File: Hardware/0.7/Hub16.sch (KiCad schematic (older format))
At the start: 97 parts, among them J1 USB_C_Receptacle_USB2.0, J2 AVR-ISP-6, K1 KEYSW, K11 KEYSW, K12 KEYSW, K13 KEYSW, K14 KEYSW, K16 KEYSW, K17 KEYSW, K18 KEYSW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

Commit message: update footprints + bom
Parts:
- C1: DigiKey 1276-1871-1-ND -> 1276-1871-1-ND; LCSC C85713 -> C85713; MPN CL10A106MP8NNNC -> CL10A106MP8NNNC; Substitue Allowed? Y -> Y - X5R or better
- C10, C11, C38, C4, C5, C6, C7, C8, C9: Substitue Allowed? Y -> Y - X5R or better
- C2, C3: value 22p -> 15p; DigiKey 1276-2228-1-ND -> 1276-1296-2-ND; LCSC C1653 -> C1644; MPN CL10C220JB8NFNC -> CL10C150JB8NNNC; Substitue Allowed? Y -> Y - NP0 / C0G or better
- C23, C27, C28, C29, C30, C31, C32, C33, C34, C35, C36, C37: DigiKey (none) -> 1276-1000-1-ND; LCSC (none) -> C1591; MPN (none) -> CL10B104KB8NNNC; Manufacturer (none) -> Samsung Electro-Mechanics; Substitue Allowed? (none) -> Y - X5R or better
- D1: DigiKey 732-4980-1-ND -> (none); MPN 150060VS75000 -> OSK40603C1E; Manufacturer Wurth Electronik -> OptoSupply; Notes LCSC: Substutite PN -> (none); Substitue Allowed? Y -> Y - Any Pink / Purple
- D10, D16, D2, D22, D23, D29, D3, D30, D31, D32, D4: LCSC C114586 -> C268294; Notes (none) -> Black prefered, but white also suitable
- D11, D12, D13, D14, D17, D18, D19, D20, D24, D25, D26, D27, D5, D6, D7, D8: Substitue Allowed? Y -> Y - Any 1N4148
- F1: LCSC C181350 -> C66452; Substitue Allowed? Y -> Y - 500mA hold / 1A trip
- FB5: DigiKey 490-1014-1-ND -> 490-5258-1-ND; LCSC C19330 -> C85833; MPN BLM18AG601SN1D -> BLM18KG601SN1D; Substitue Allowed? Y -> Y - 600R, > 1A current
- J1: Substitue Allowed? Y -> Y - Footprint / pinout compatiable
- R1: DigiKey CR0603-JW-222ELFCT-ND -> 118-CR0603-JW-512ELFCT-ND; LCSC C113303 -> C14677; MPN CR0603-JW-222ELF -> CR0603-JW-512ELF; Substitue Allowed? Y -> Y - Same spec
- R11, R2, R3, R4, R5, R6, R7, R8, RN1, RN3: Substitue Allowed? Y -> Y - Same spec
- SW1: value KMR2 -> EVQPUL; DigiKey 401-1704-1-ND -> P10853SCT-ND; LCSC C354946 -> C397351; MPN KSR223GLFG -> EVQ-PUL02K; Manufacturer C&K -> Panasonic; Substitue Allowed? Y -> Y - Same footprint
- SW2, SW3: DigiKey 987-1398-ND -> PEC11L-4120F-S0020-ND; LCSC C361165 -> (none); MPN EC11E1834403 -> PEC11L-4120F-S0020; Manufacturer (none) -> Bourns; Substitue Allowed? Y -> Y - 20 PPR
- U2: DigiKey ATMEGA32U4-AURCT-ND -> ATMEGA32U4-MU-ND; LCSC C44854 -> C45874; MPN ATMEGA32U4-AU -> ATMEGA32U4-MU
- Y1: DigiKey 535-9134-1-ND -> 535-9675-6-ND; LCSC C179641 -> C164044; MPN ABM8-16.000MHZ-B2-T -> ABM8-16.000MHZ-10-1-U-T; Notes (none) -> LCSC: Substitute PN; Substitue Allowed? Y -> Y - 16 MHz, 10/12pF

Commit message: add note on uncommenting out code
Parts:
- C2, C3: Substitue Allowed? Y - NP0 / C0G or better -> Y - NP0 / C0G
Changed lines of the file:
@@
 F 4 "1276-1296-2-ND" H 2875 3325 50  0001 C CNN "DigiKey"
 F 5 "CL10C150JB8NNNC" H 2875 3325 50  0001 C CNN "MPN"
-F 6 "Y - NP0 / C0G or better" H 2875 3325 50  0001 C CNN "Substitue Allowed?"
+F 6 "Y - NP0 / C0G" H 2875 3325 50  0001 C CNN "Substitue Allowed?"
 F 7 "C1644" H 2875 3325 50  0001 C CNN "LCSC"
 F 8 "Samsung Electro-Mechanics" H 2875 3325 50  0001 C CNN "Manufacturer"
@@
 F 4 "1276-1296-2-ND" H 2875 2925 50  0001 C CNN "DigiKey"
 F 5 "CL10C150JB8NNNC" H 2875 2925 50  0001 C CNN "MPN"
-F 6 "Y - NP0 / C0G or better" H 2875 2925 50  0001 C CNN "Substitue Allowed?"
+F 6 "Y - NP0 / C0G" H 2875 2925 50  0001 C CNN "Substitue Allowed?"
 F 7 "C1644" H 2875 2925 50  0001 C CNN "LCSC"
 F 8 "Samsung Electro-Mechanics" H 2875 2925 50  0001 C CNN "Manufacturer"

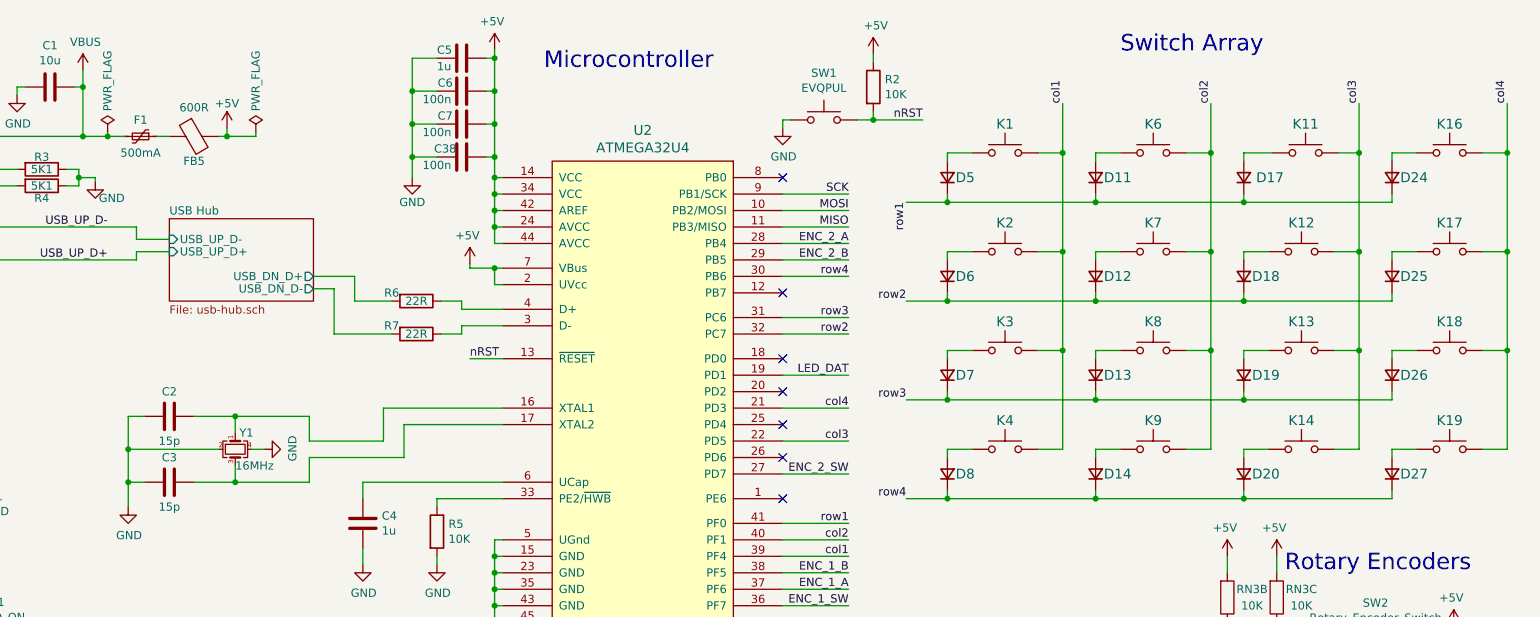
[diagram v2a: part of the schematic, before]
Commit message: update fuse values
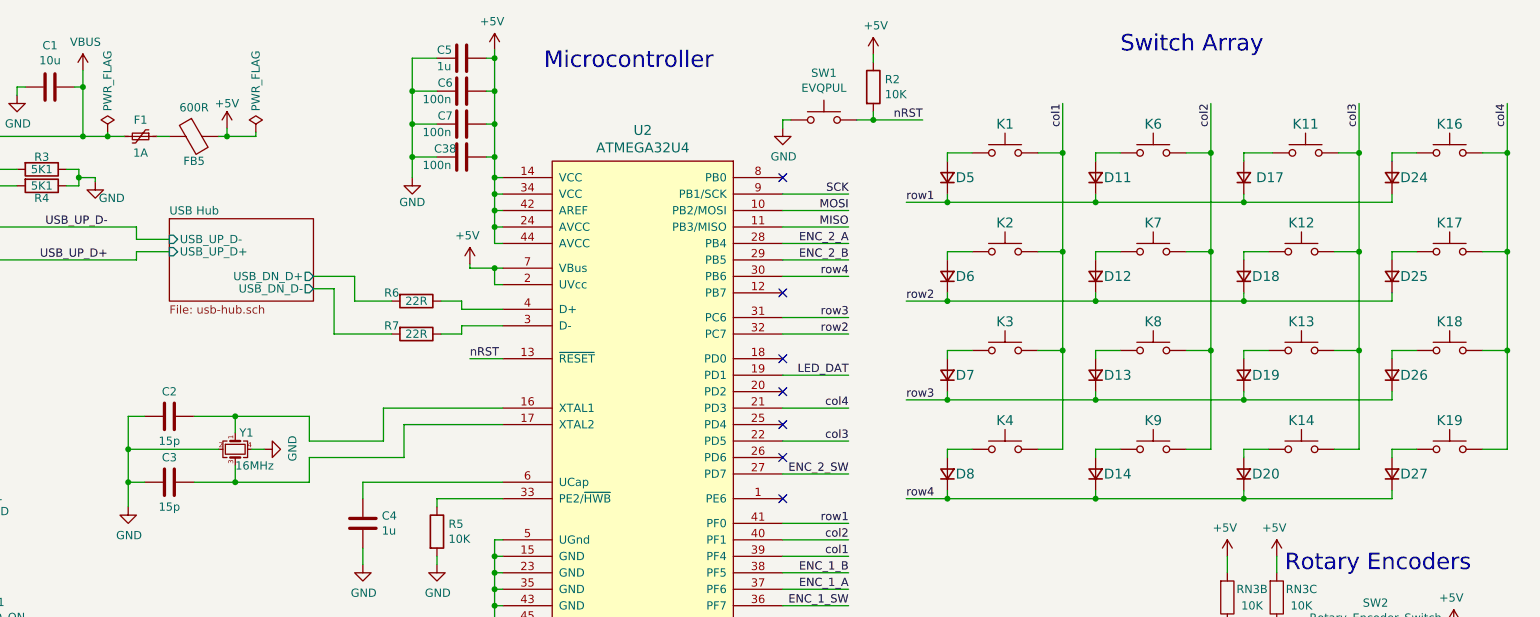
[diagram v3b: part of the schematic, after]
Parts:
- D1: Notes (none) -> Cannot source from DigiKey
- F1: value 500mA -> 1A; DigiKey 507-1813-1-ND -> F2774CT-ND; LCSC C66452 -> C80270; MPN 0ZCK0050FF2E -> 0805L100WR; Manufacturer Bel Fuse -> Littelfuse; Notes LCSC: Substitute PN -> (none); Substitue Allowed? Y - 500mA hold / 1A trip -> Y - 1A hold / >1.5A trip
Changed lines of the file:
@@
 	8500 2825 9400 2825
 Connection ~ 9400 2825
-Text Label 7350 2825 2    50   ~ 0
+Text Label 7350 2825 0    50   ~ 0
 row3
 Text Notes 8650 725  0    100  ~ 0
@@
 row4
 Connection ~ 2625 3325
-Text Label 11000 1025 1    50   ~ 0
+Text Label 11000 1025 3    50   ~ 0
 col4
-Text Label 10100 1025 1    50   ~ 0
+Text Label 10100 1025 3    50   ~ 0
 col3
-Text Label 9200 1025 1    50   ~ 0
+Text Label 9200 1025 3    50   ~ 0
 col2
-Text Label 8300 1025 1    50   ~ 0
+Text Label 8300 1025 3    50   ~ 0
 col1
 $Comp
@@
 Wire Wire Line
 	7600 1925 7600 1975
-Text Label 7350 2225 2    50   ~ 0
+Text Label 7350 2225 0    50   ~ 0
 row2
 Connection ~ 9400 2225
@@
 Wire Wire Line
 	7600 1325 7600 1375
-Text Label 7350 1625 3    50   ~ 0
+Text Label 7350 1625 0    50   ~ 0
 row1
 Connection ~ 9400 1625
@@
 Wire Wire Line
 	7600 3125 7600 3175
-Text Label 7350 3425 2    50   ~ 0
+Text Label 7350 3425 0    50   ~ 0
 row4
 Wire Wire Line
@@
 F 8 "C364559" H 1650 3450 50  0001 C CNN "LCSC"
 F 9 "OptoSupply" H 1650 3450 50  0001 C CNN "Manufacturer"
-F 10 "" H 1650 3450 50  0001 C CNN "Notes"
+F 10 "Cannot source from DigiKey" H 1650 3450 50  0001 C CNN "Notes"
 	1    1650 3450
 	0    -1   -1   0
@@
 AR Path="/5E5406D9/5EB49DDF" Ref="F?"  Part="1"
 F 0 "F1" V 2600 1225 50  0000 C CNN
-F 1 "500mA" V 2800 1225 50  0000 C CNN
+F 1 "1A" V 2800 1225 50  0000 C CNN
 F 2 "josh-passives-smt:Fuse_0805_2012Metric" H 2750 1025 50  0001 L CNN
 F 3 "~" H 2700 1225 50  0001 C CNN
-F 4 "C66452" H 2700 1225 50  0001 C CNN "LCSC"
-F 5 "0ZCK0050FF2E" H 2700 1225 50  0001 C CNN "MPN"
-F 6 "507-1813-1-ND" H 2700 1225 50  0001 C CNN "DigiKey"
-F 7 "LCSC: Substitute PN" H 2700 1225 50  0001 C CNN "Notes"
-F 8 "Y - 500mA hold / 1A trip" H 2700 1225 50  0001 C CNN "Substitue Allowed?"
-F 9 "Bel Fuse" H 2700 1225 50  0001 C CNN "Manufacturer"
+F 4 "C80270" H 2700 1225 50  0001 C CNN "LCSC"
+F 5 "0805L100WR" H 2700 1225 50  0001 C CNN "MPN"
+F 6 "F2774CT-ND " H 2700 1225 50  0001 C CNN "DigiKey"
+F 7 "" H 2700 1225 50  0001 C CNN "Notes"
+F 8 "Y - 1A hold / >1.5A trip" H 2700 1225 50  0001 C CNN "Substitue Allowed?"
+F 9 "Littelfuse" H 2700 1225 50  0001 C CNN "Manufacturer"
 	1    2700 1225
 	0    1    1    0
